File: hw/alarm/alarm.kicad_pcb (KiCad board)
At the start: 2 copper layers, 71 x 73 mm, 68 parts, among them IC3 SHT40-BD1B-R2, IC5 PEC11S-929K-S0015, IC6 MAX31328NELB+, J1 4328, J2 FFC2B35-24-T, J3 975, Q1 DMG2305UX-7, Q2 2SC5585TL, Q3 Si1308EDL-T1-GE3, Q4 DMG2305UX-7, U1 RaspberryPi_Pico, U4 AS1115-BSST, U5 TDCR1060M

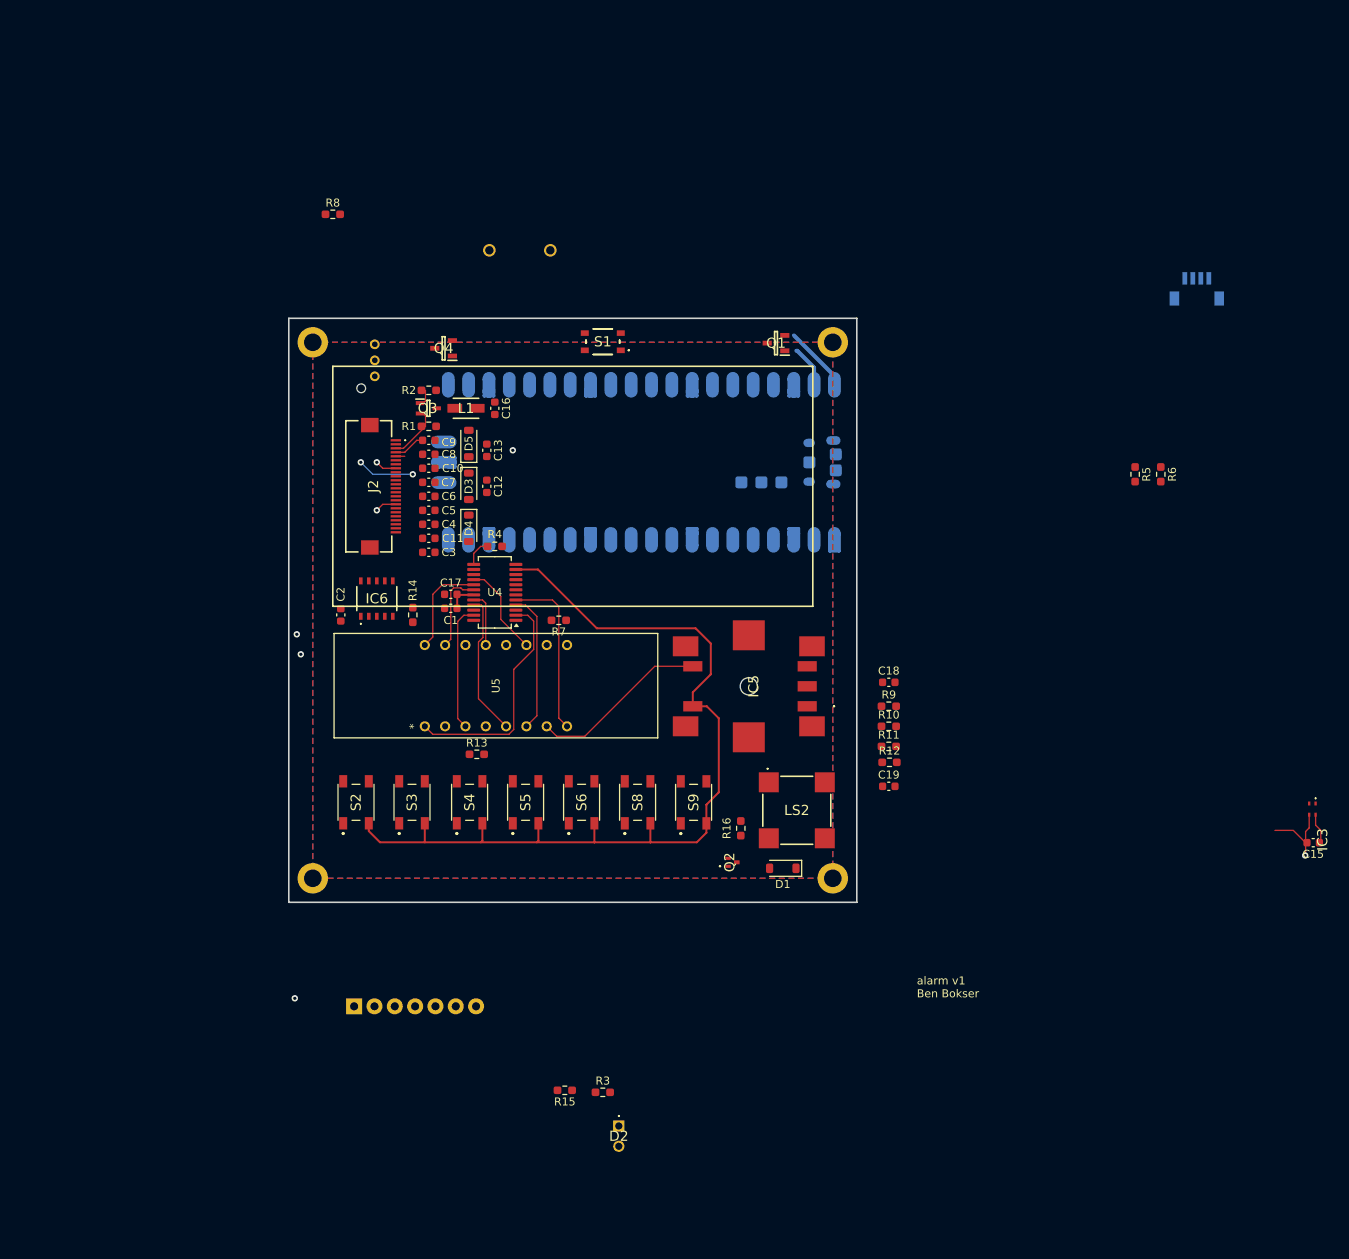
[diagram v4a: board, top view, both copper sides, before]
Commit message: Finish most of board layout
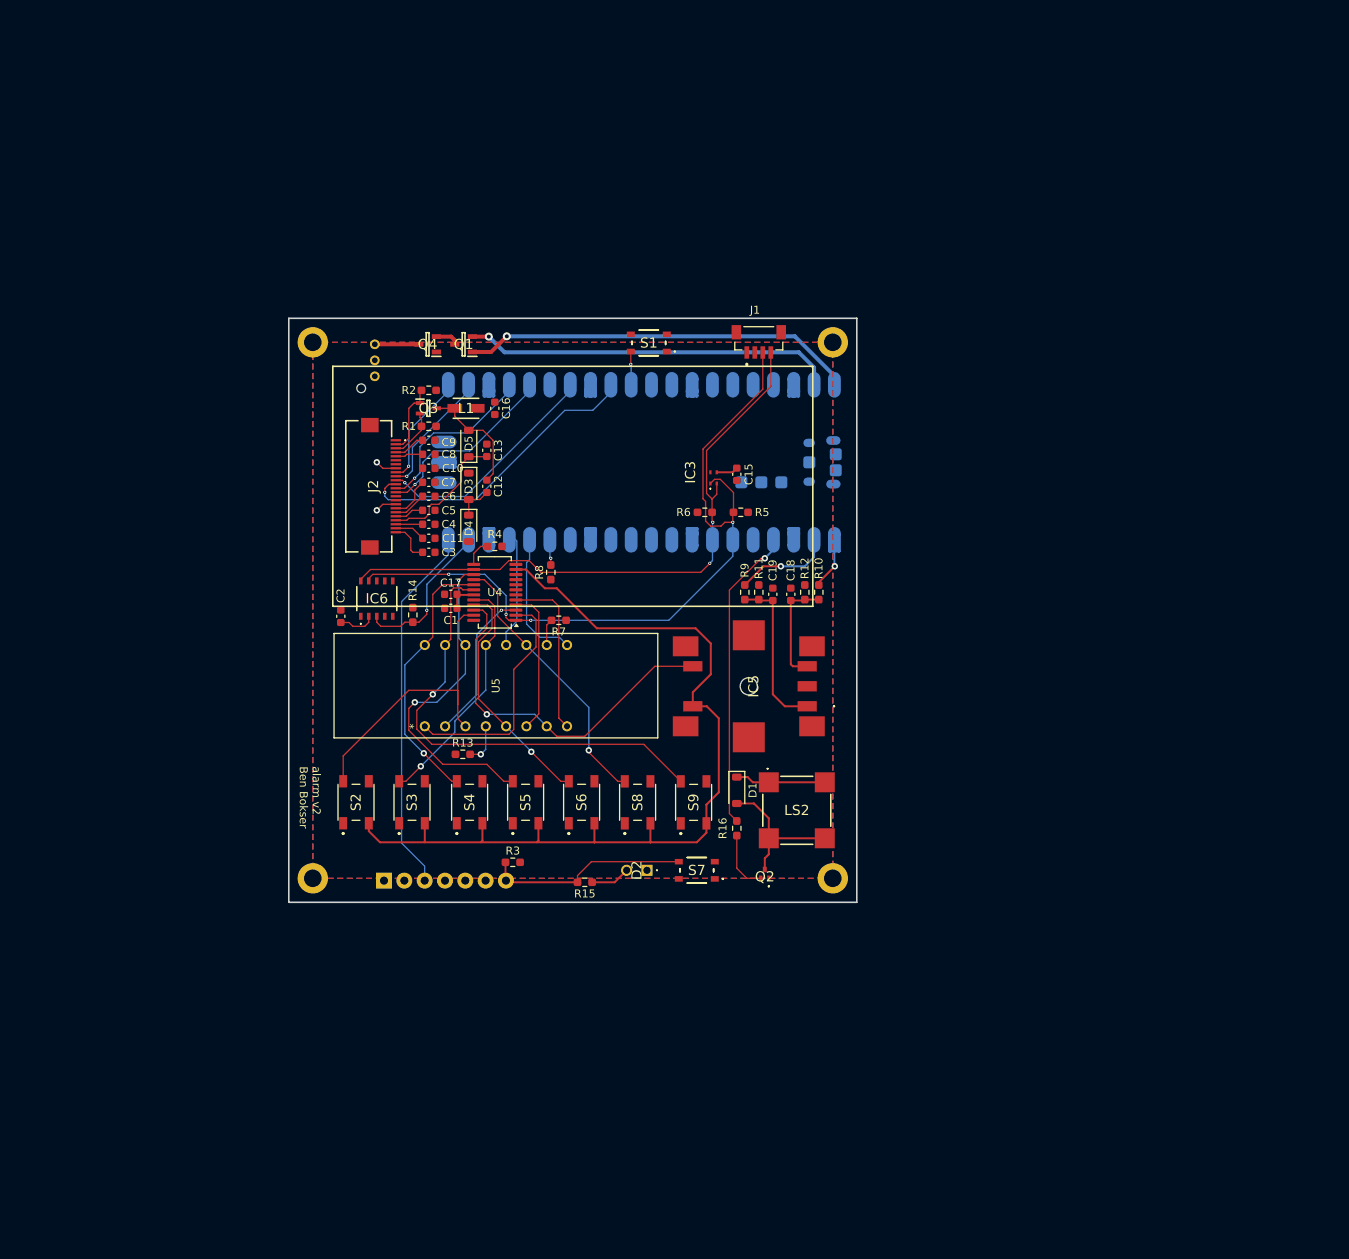
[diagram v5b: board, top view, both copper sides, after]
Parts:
- J1: moved to F.Cu
- S7: value DS01-254-L-01BE -> RKB2SJK250SMTR_LFS; footprint SamacSys_Parts:DS01254L01BE -> SamacSys_Parts:RKB2SJK250SMTRLFS; moved to F.Cu
- moved IC3 85.5 mm to (175.6, 81.5), turned to 90 degrees
- moved C15 85.5 mm to (178.5, 81.0), turned to -90 degrees
- moved S7 81.7 mm to (173.5, 130.5), turned to 180 degrees
- moved R6 57.2 mm to (174.5, 85.8), turned to 0 degrees
- moved J1 55.0 mm to (181.2, 64.0)
- moved R8 52.4 mm to (155.2, 93.2), turned to 90 degrees
- moved R5 49.5 mm to (179.0, 85.8), turned to 180 degrees
- moved Q1 39.1 mm to (144.3, 64.8)
- moved D2 32.2 mm to (167.3, 130.5), turned to -90 degrees
- moved R3 30.9 mm to (150.5, 129.5)
- moved C19 28.0 mm to (183.0, 96.0), turned to -90 degrees
- moved R15 26.1 mm to (159.5, 132.0)
- moved R11 25.2 mm to (181.2, 95.8), turned to -90 degrees
- moved R12 23.7 mm to (187.0, 95.8), turned to -90 degrees
- moved R9 23.0 mm to (179.5, 95.8), turned to -90 degrees
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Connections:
- A1 pad 7: /RF_key -> Net-(A1-KEY)
- R15 pad 2: /RF_key -> Net-(A1-KEY)
- R3 pad 1: /RF_key -> Net-(A1-KEY)
- S7 pad 1: GND -> unconnected-(S7-COM_1-Pad1)
- S7 pad 2: Net-(S7-NO) -> +3.3V
- U1 pad 1: unconnected-(U1-GPIO0-Pad1) -> /Enc_B1
- U1 pad 10: /EinkCS -> unconnected-(U1-GPIO7-Pad10)
- U1 pad 11: /Enc_A1 -> unconnected-(U1-GPIO8-Pad11)
- U1 pad 12: /Enc_B1 -> unconnected-(U1-GPIO9-Pad12)
- U1 pad 14: Net-(S7-NO) -> unconnected-(U1-GPIO10-Pad14)
- U1 pad 2: unconnected-(U1-GPIO1-Pad2) -> /Enc_A1
- U1 pad 20: /Buzzer -> /RF1
- U1 pad 21: /EinkRESET -> /EinkBUSY
- U1 pad 22: /EinkBUSY -> /EinkRESET
- U1 pad 26: /MISO -> unconnected-(U1-GPIO20-Pad26)
- U1 pad 29: unconnected-(U1-GPIO22-Pad29) -> /EinkCS
- U1 pad 4: /RF_key -> /Buzzer
- U1 pad 5: /RF1 -> unconnected-(U1-GPIO3-Pad5)
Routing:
- net /SDA: track 0.00 -> 93.3 mm, vias 0 -> 4
- net /SCL: track 0.10 -> 78.2 mm, vias 1 -> 2
- net Net-(U4-SEGG): track 10.2 -> 57.9 mm, vias 0 -> 1
- net /RF1: track 0.00 -> 47.0 mm
- net Net-(U4-SEGA): track 0.00 -> 41.4 mm, vias 0 -> 2
- net Net-(Q1-S): track 6.04 -> 47.3 mm, vias 0 -> 1
- net Net-(Q1-G): track 9.07 -> 50.0 mm, vias 0 -> 1
- net /Buzzer: track 0.00 -> 38.9 mm, vias 0 -> 1
- net /EinkCS: track 0.00 -> 36.7 mm, vias 0 -> 1
- net /DC: track 0.00 -> 28.1 mm, vias 0 -> 1
- net Net-(A1-KEY): track 0.00 -> 25.6 mm
- net /Enc_E: track 22.4 -> 46.0 mm, vias 0 -> 1
- net Net-(U4-SEGC): track 6.90 -> 30.3 mm, vias 0 -> 1
- net /MOSI: track 0.00 -> 23.0 mm, vias 0 -> 1
- net Net-(U4-SEGF): track 11.7 -> 34.3 mm, vias 0 -> 1
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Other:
- board text added: "alarm v2 Ben Bokser"
- board text removed: "alarm v1 Ben Bokser"

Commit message: Finish board layout pending last checks
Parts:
- moved J1 71.1 mm to (125.0, 107.5), turned to 90 degrees
- moved C15 4.30 mm to (176.0, 77.5), turned to 90 degrees
- moved C2 0.25 mm to (129.0, 99.0)
- turned C16 to 90 degrees
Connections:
- J3 pad 1: GND -> Net-(J3-+)
- J3 pad 3: Net-(J3-+) -> GND
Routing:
- net GND: track 5.12 -> 107.4 mm, vias 2 -> 19
- net +3.3V: track 22.5 -> 40.3 mm, vias 0 -> 1
- net /IRQ: track 3.99 -> 20.1 mm, vias 1 -> 3
- net /SDA: track 93.3 -> 81.7 mm
- net /SCL: track 78.2 -> 67.4 mm
- net /VGL: track 3.86 -> 10.1 mm
- net /EinkRESET: track 15.2 -> 19.9 mm
- net /DC: track 28.1 -> 31.9 mm
- net Net-(J3-+): track 5.50 -> 7.16 mm
- net /Enc_A1: track 13.1 -> 12.1 mm

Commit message: Further tweaks & corrections, create production files
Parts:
- removed IC5: PEC11S-929K-S0015, SamacSys_Parts:PEC11S929KS0015
- removed J1: 4328, 4328:ADAFRUIT_4328
- removed REF** (x4): MountingHole_2.2mm_M2_DIN965_Pad, MountingHole:MountingHole_2.2mm_M2_DIN965_Pad
- added H1: MountingHole_Pad, MountingHole:MountingHole_2.7mm_M2.5_DIN965_Pad, F.Cu at (190.5, 64.5)
- added H2: MountingHole_Pad, MountingHole:MountingHole_2.7mm_M2.5_DIN965_Pad, F.Cu at (190.5, 131.5)
- added H3: MountingHole_Pad, MountingHole:MountingHole_2.7mm_M2.5_DIN965_Pad, F.Cu at (125.5, 64.5)
- added H4: MountingHole_Pad, MountingHole:MountingHole_2.7mm_M2.5_DIN965_Pad, F.Cu at (125.5, 131.5)
- added J4: SM04B-SRSS-TB_LF__SN__P_, SamacSys_Parts:SM04BSRSSTBLFSNP, F.Cu at (176.0, 65.2)
- added U2: PEC11R-4215F-S0024, SamacSys_Parts:PEC11R4215FS0024, F.Cu at (173.0, 110.0)
- moved IC6 35.8 mm to (167.0, 84.0), turned to -90 degrees
- moved C2 35.5 mm to (162.0, 86.0), turned to -90 degrees
- moved R14 29.2 mm to (162.0, 82.0)
- moved C15 19.6 mm to (174.3, 97.0), turned to 0 degrees
- moved IC3 12.4 mm to (174.4, 93.8), turned to -90 degrees
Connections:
- U1 pad 14: unconnected-(U1-GPIO10-Pad14) -> /RTC_INT
- U1 pad 19: /RTC_INT -> unconnected-(U1-GPIO14-Pad19)
- U1 pad 27: /DC -> /EinkCS
- U1 pad 29: /EinkCS -> /DC
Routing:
- net /DC: track 31.9 -> 42.5 mm
- net /SDA: track 81.7 -> 71.9 mm, vias 4 -> 3
- net /RTC_INT: track 20.1 -> 11.3 mm
- net +3.3V: track 40.3 -> 34.7 mm
- net /SCL: track 67.4 -> 62.5 mm, vias 2 -> 3
- net /EinkCS: track 36.7 -> 32.6 mm
- net /VGL: track 10.1 -> 12.6 mm
- net GND: track 107.4 -> 109.7 mm
- net Net-(U2-CHANNEL_A): track 20.2 -> 18.6 mm
- net Net-(U4-SEGD): track 38.5 -> 39.6 mm
- net Net-(U2-CHANNEL_B): track 13.7 -> 12.6 mm
- net Net-(Q1-S): track 47.3 -> 46.4 mm
- net Net-(U4-DIG3): track 21.1 -> 20.4 mm
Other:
- outline, holes or cut-outs redrawn

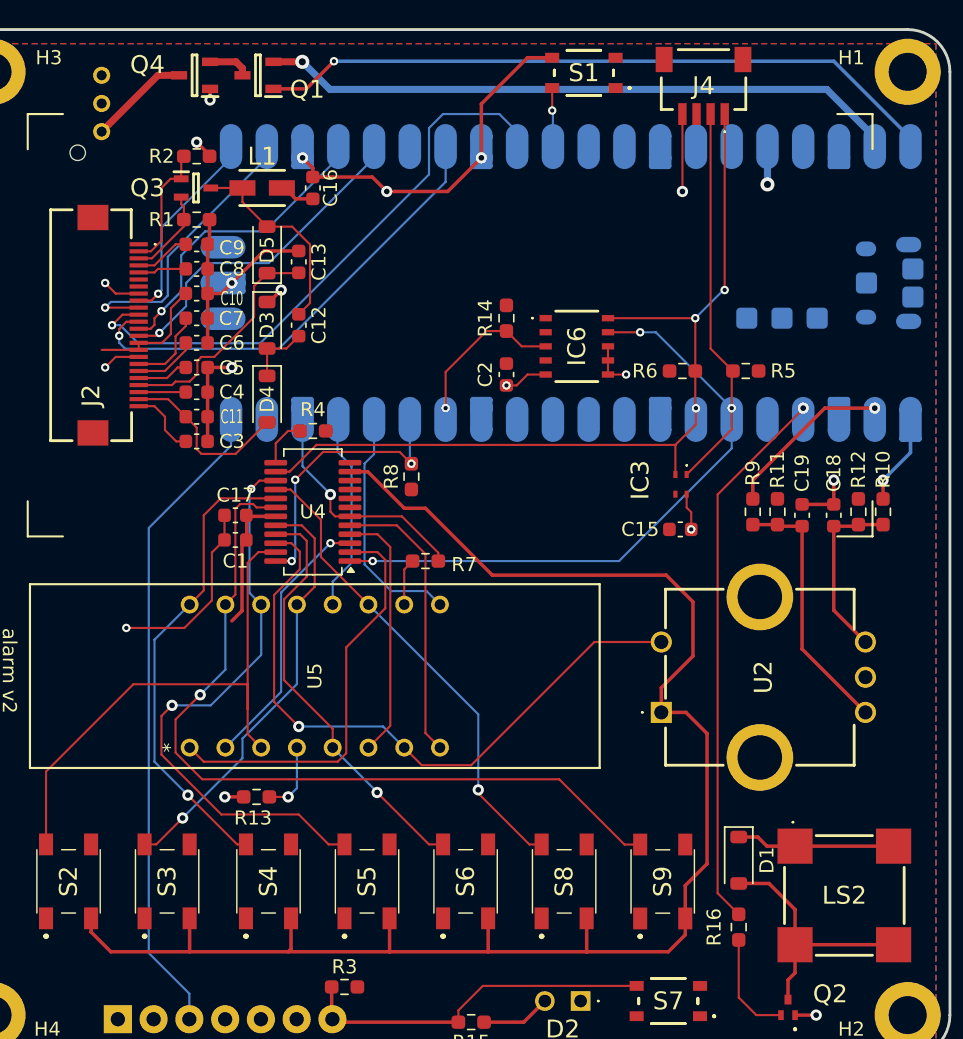
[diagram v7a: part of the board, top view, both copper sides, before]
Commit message: Add connectors for unused pins
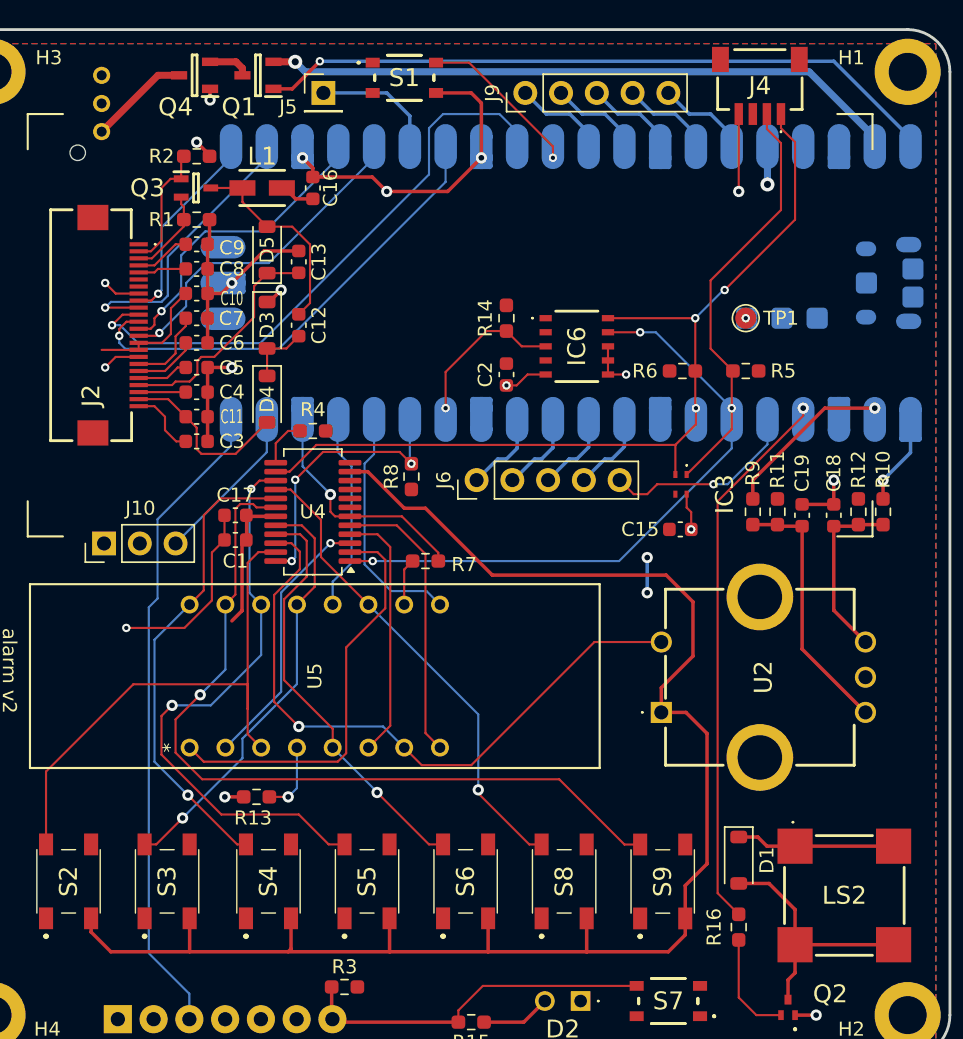
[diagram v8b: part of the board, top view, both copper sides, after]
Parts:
- added J10: Conn_01x03, Connector_PinHeader_2.54mm:PinHeader_1x03_P2.54mm_Vertical, F.Cu at (133.4, 98.0)
- added J5: Conn_01x01_Pin, Connector_PinHeader_2.54mm:PinHeader_1x01_P2.54mm_Vertical, F.Cu at (149.0, 66.0)
- added J6: Conn_01x05, Connector_PinHeader_2.54mm:PinHeader_1x05_P2.54mm_Vertical, F.Cu at (159.9, 93.5)
- added J9: Conn_01x05, Connector_PinHeader_2.54mm:PinHeader_1x05_P2.54mm_Vertical, F.Cu at (163.3, 66.0)
- added TP1: TestPoint, TestPoint:TestPoint_Pad_D1.5mm, F.Cu at (179.0, 82.0)
- moved S1 12.8 mm to (154.8, 64.9), turned to 0 degrees
- moved J4 4.00 mm to (180.0, 65.2)
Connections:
- U1 pad 10: unconnected-(U1-GPIO7-Pad10) -> Net-(J6-Pin_3)
- U1 pad 11: unconnected-(U1-GPIO8-Pad11) -> Net-(J6-Pin_2)
- U1 pad 12: unconnected-(U1-GPIO9-Pad12) -> Net-(J6-Pin_1)
- U1 pad 19: unconnected-(U1-GPIO14-Pad19) -> Net-(J10-Pin_3)
- U1 pad 26: unconnected-(U1-GPIO20-Pad26) -> Net-(J5-Pin_1)
- U1 pad 31: unconnected-(U1-GPIO26_ADC0-Pad31) -> Net-(J9-Pin_1)
- U1 pad 32: unconnected-(U1-GPIO27_ADC1-Pad32) -> Net-(J9-Pin_2)
- U1 pad 33: unconnected-(U1-AGND-Pad33) -> Net-(J9-Pin_3)
- U1 pad 34: unconnected-(U1-GPIO28_ADC2-Pad34) -> Net-(J9-Pin_4)
- U1 pad 35: unconnected-(U1-ADC_VREF-Pad35) -> Net-(J9-Pin_5)
- U1 pad 5: unconnected-(U1-GPIO3-Pad5) -> Net-(J6-Pin_5)
- U1 pad 9: unconnected-(U1-GPIO6-Pad9) -> Net-(J6-Pin_4)
- U1 pad TP6: unconnected-(U1-~{BOOTSEL}-PadTP6) -> Net-(U1-~{BOOTSEL})
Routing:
- net Net-(J6-Pin_5): track 0.00 -> 15.0 mm, vias 0 -> 1
- net Net-(J10-Pin_3): track 0.00 -> 12.3 mm
- net Net-(J5-Pin_1): track 0.00 -> 9.79 mm
- net Net-(J9-Pin_1): track 0.00 -> 7.45 mm
- net Net-(J9-Pin_2): track 0.00 -> 7.42 mm
- net Net-(J9-Pin_3): track 0.00 -> 7.39 mm
- net Net-(J9-Pin_4): track 0.00 -> 7.38 mm
- net Net-(J9-Pin_5): track 0.00 -> 7.35 mm
- net Net-(J6-Pin_1): track 0.00 -> 6.67 mm
- net Net-(J6-Pin_2): track 0.00 -> 6.64 mm
- net Net-(J6-Pin_3): track 0.00 -> 6.62 mm
- net Net-(J6-Pin_4): track 0.00 -> 6.60 mm
- net Net-(S1-COM_2): track 4.98 -> 11.6 mm
- net GND: track 109.7 -> 106.9 mm
- net +3.3V: track 34.7 -> 37.2 mm, vias 1 -> 3
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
